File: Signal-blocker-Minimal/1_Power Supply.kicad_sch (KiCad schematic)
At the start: 7 parts, among them U8 A0509S-1WR3

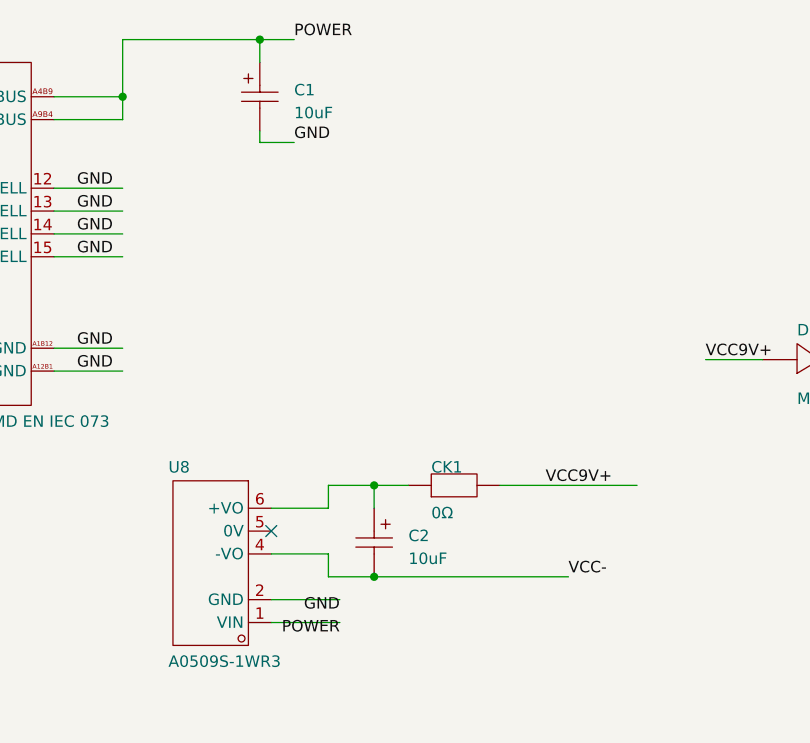
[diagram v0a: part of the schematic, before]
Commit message: Version 2.1 Update！
Fix some circuit!
More stabler!
Replace all the restrictor and capacitor into 0603 packaging!
create BOM excel,Bill of Material.
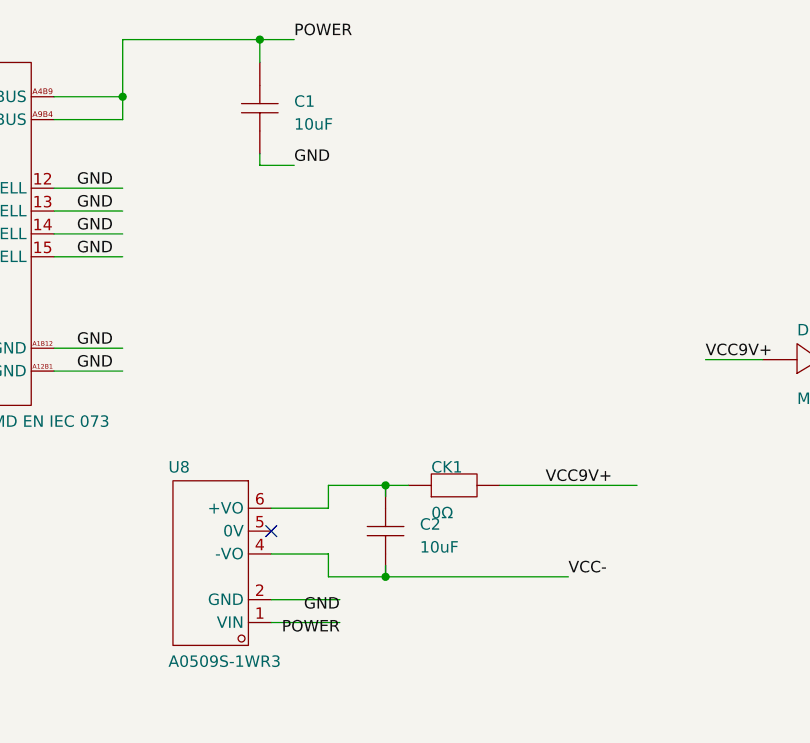
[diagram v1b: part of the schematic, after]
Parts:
- removed ?: (no value), ProPrj_Sig-easyedapro:, symbol ProPrj_Sig-easyedapro:Drawing-Symbol_A4
- removed C1, C2: 10uF, ProPrj_Sig-easyedapro:CAP-SMD_L3.2-W1.6-RD-C7171, symbol ProPrj_Sig-easyedapro:TAJA106K016RNJ
- removed CK1: 0Ω, ProPrj_Sig-easyedapro:R0603, symbol ProPrj_Sig-easyedapro:0Ω
- removed D1: MM1W5V1, ProPrj_Sig-easyedapro:SOD-123_L2.7-W1.6-LS3.7-RD, symbol ProPrj_Sig-easyedapro:MM1W5V1
- removed U8: A0509S-1WR3, ProPrj_Sig-easyedapro:PWRM-TH_A05XXS-1WR3, symbol ProPrj_Sig-easyedapro:A0509S-1WR3_C5369385
- removed USB1: TYPE-C 16PIN 3MD EN IEC 073, ProPrj_Sig-easyedapro:TYPE-C-SMD_HDGC_TYPE-C-ZL-104PWB, symbol ProPrj_Sig-easyedapro:TYPE-C 16PIN 3MD EN IEC 073
- added ?: (no value), Signal-blo-easyedapro:, symbol Signal-blo-easyedapro:Drawing-Symbol_A4
- added C1, C2: 10uF, Signal-blo-easyedapro:C0603, symbol Signal-blo-easyedapro:HGC0603R5106M160NTHJ
- added CK1: 0Ω, Signal-blo-easyedapro:R0603, symbol Signal-blo-easyedapro:0Ω
- added D1: MM1W5V1, Signal-blo-easyedapro:SOD-123_L2.7-W1.6-LS3.7-RD, symbol Signal-blo-easyedapro:MM1W5V1
- added U8: A0509S-1WR3, Signal-blo-easyedapro:PWRM-TH_A05XXS-1WR3, symbol Signal-blo-easyedapro:A0509S-1WR3_C5369385
- added USB1: TYPE-C 16PIN 3MD EN IEC 073, Signal-blo-easyedapro:TYPE-C-SMD_HDGC_TYPE-C-ZL-104PWB, symbol Signal-blo-easyedapro:TYPE-C 16PIN 3MD EN IEC 073
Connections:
- net GND: now also C1.1, U8.2 (GND), USB1.12 (SHELL), USB1.13 (SHELL), USB1.14 (SHELL), USB1.15 (SHELL), USB1.A12B1 (GND), USB1.A1B12 (GND)
- net POWER: now also C1.2, U8.1 (VIN), USB1.A4B9 (VBUS), USB1.A9B4 (VBUS)
- net VCC+: now also D1.1 (C)
- net VCC-: now also C2.1, U8.4 (-VO)
- net VCC9V+: now also CK1.2, D1.2 (A)
- new net: C2.2, CK1.1, U8.6 (+VO)
